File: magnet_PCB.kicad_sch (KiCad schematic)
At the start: 0 parts

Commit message: Add LED strip subsheet and place all components
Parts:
- added BT1: Battery_Cell, symbol Device:Battery_Cell
- added LS1: Speaker, symbol Device:Speaker
- added M5: Motor_DC_ALT, symbol Motor:Motor_DC_ALT
- added RV2: R_Potentiometer_Trim, symbol Device:R_Potentiometer_Trim
- added U1: DRV8833PW, Package_SO:TSSOP-16_4.4x5mm_P0.65mm, symbol Driver_Motor:DRV8833PW
- added U2: MAX98306xDT, Package_DFN_QFN:TDFN-14-1EP_3x3mm_P0.4mm_EP1.78x2.35mm, symbol Amplifier_Audio:MAX98306xDT
- added U3: ESP32-S3, Package_DFN_QFN:QFN-56-1EP_7x7mm_P0.4mm_EP4x4mm, symbol MCU_Espressif:ESP32-S3
- added U4: HC-SR04, Sensor-Ultrasonic:XCVR_HC-SR04, symbol HC-SR04:HC-SR04
- added U5: LT1085-3.3, Package_TO_SOT_SMD:TO-263-2, symbol Regulator_Linear:LT1085-3.3
- added U6: LM2596S-5, Package_TO_SOT_SMD:TO-263-5_TabPin3, symbol Regulator_Switching:LM2596S-5
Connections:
- new net: U2.1 (PGND), U2.15 (PGND), U2.8 (PGND)
- new net: U2.11 (PVDD), U2.12 (PVDD)
- new net: U3.2 (VDD3P3), U3.3 (VDD3P3)
- new net: U3.55 (VDDA), U3.56 (VDDA)
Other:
- added sheet LED_Strip_8 (LED_Strip_8.kicad_sch)

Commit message: Wired LED strip
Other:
- moved on the sheet: BT1
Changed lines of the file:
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@@
 	(symbol
 		(lib_id "Device:Battery_Cell")
-		(at 81.28 161.29 0)
+		(at 57.15 146.05 0)
 		(unit 1)
 		(exclude_from_sim no)
@@
 		(fields_autoplaced yes)
 		(property "Reference" "BT1"
-			(at 85.09 158.1784 0)
+			(at 60.96 142.9384 0)
 			(effects
 				(font
@@
 		)
 		(property "Value" "Battery_Cell"
-			(at 85.09 160.7184 0)
+			(at 60.96 145.4784 0)
 			(effects
 				(font
@@
 		)
 		(property "Footprint" ""
-			(at 81.28 159.766 90)
+			(at 57.15 144.526 90)
 			(effects
 				(font
@@
 		)
 		(property "Datasheet" "~"
-			(at 81.28 159.766 90)
+			(at 57.15 144.526 90)
 			(effects
 				(font
@@
 		)
 		(property "Description" "Single-cell battery"
-			(at 81.28 161.29 0)
+			(at 57.15 146.05 0)
 			(effects
 				(font

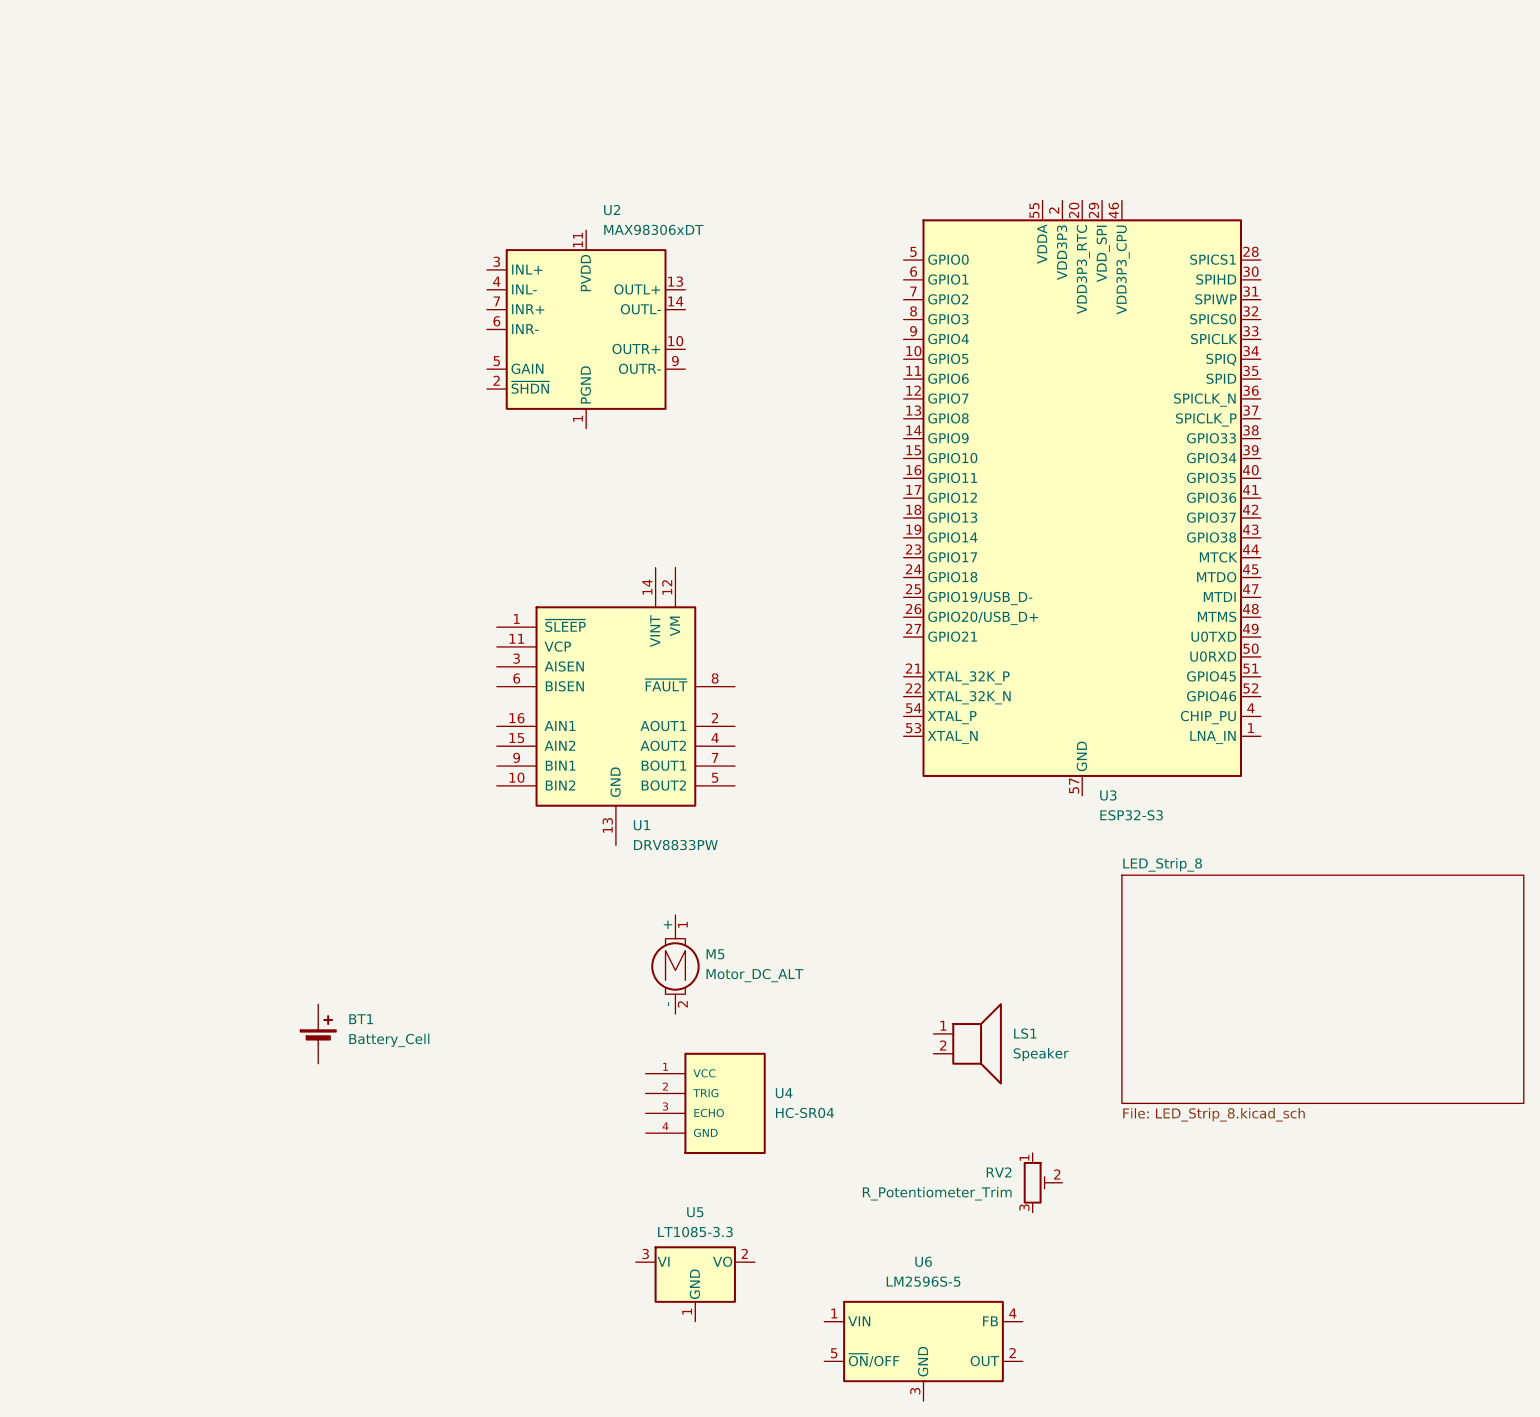
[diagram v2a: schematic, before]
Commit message: Added regulators
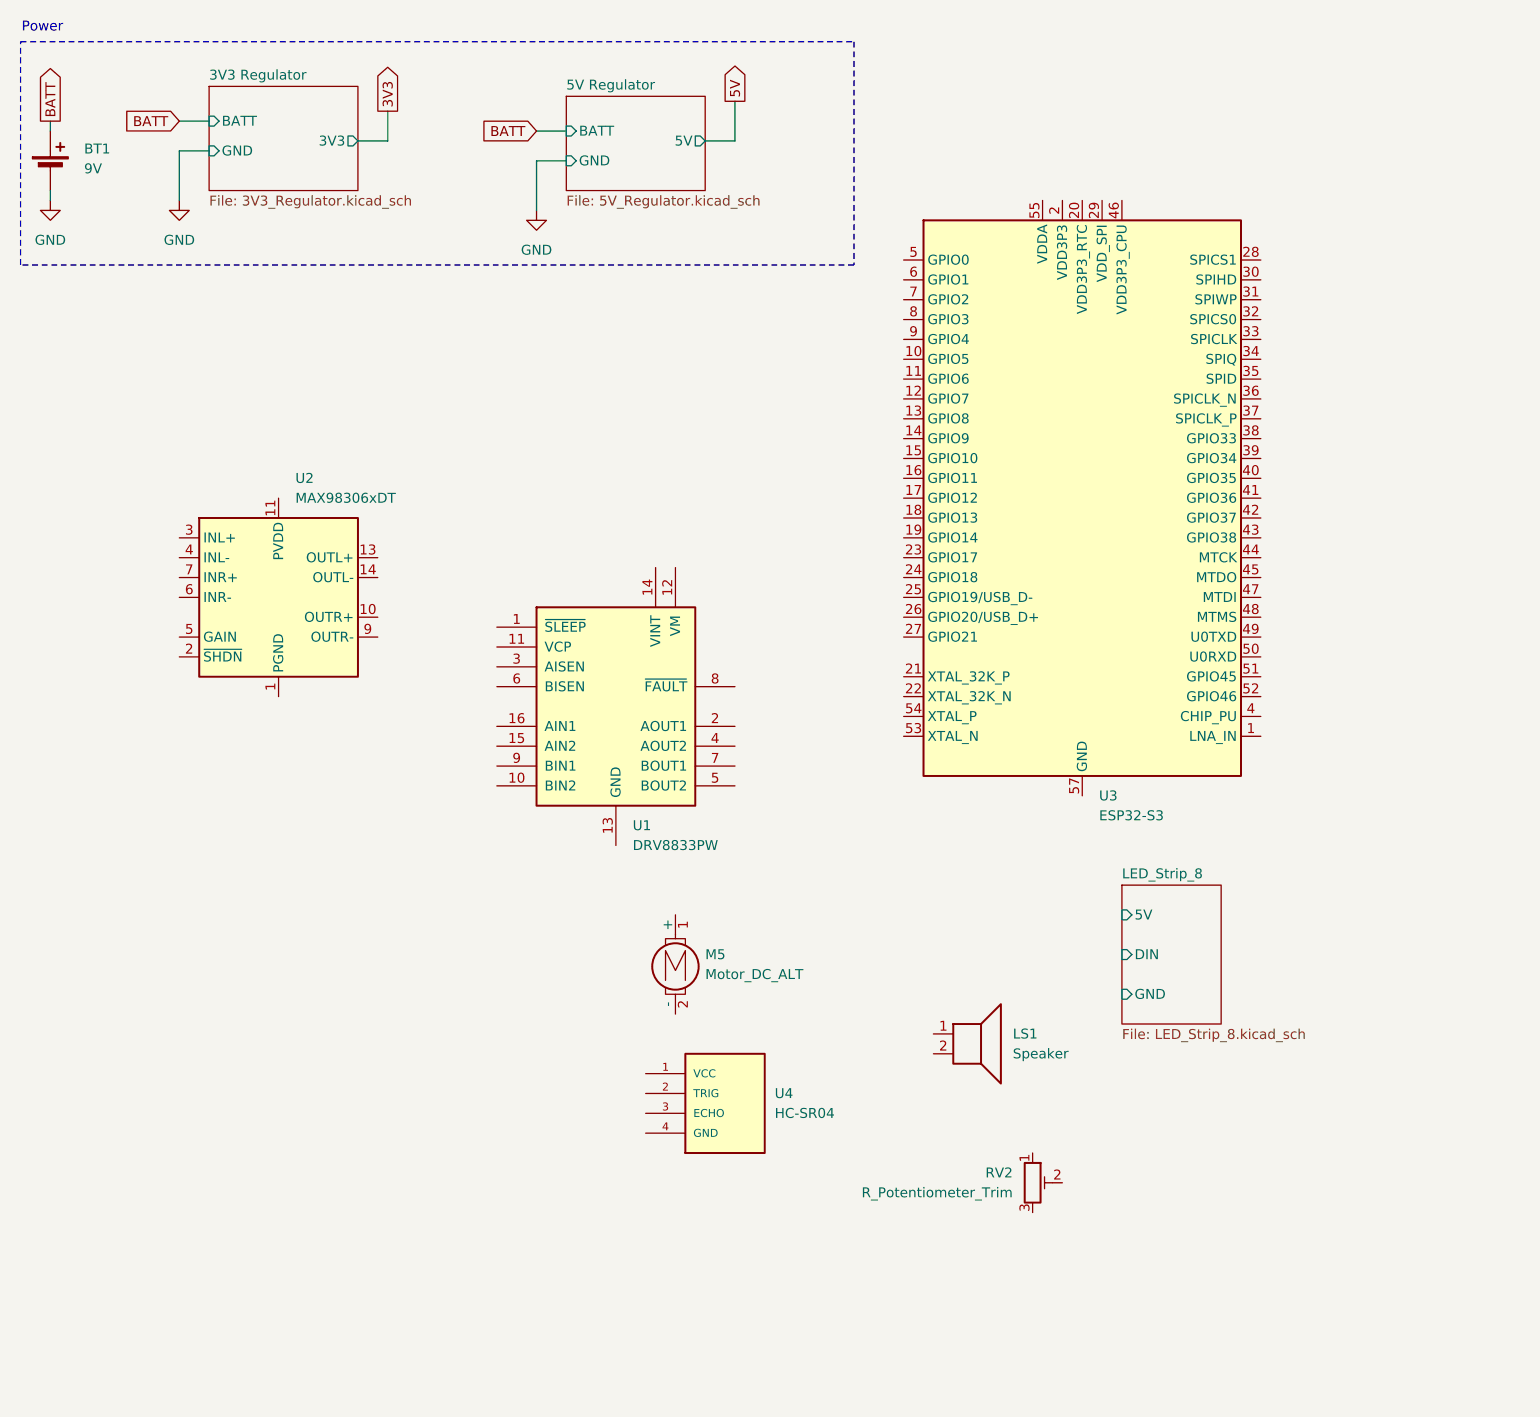
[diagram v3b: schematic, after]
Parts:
- removed U5: LT1085-3.3, Package_TO_SOT_SMD:TO-263-2, symbol Regulator_Linear:LT1085-3.3
- removed U6: LM2596S-5, Package_TO_SOT_SMD:TO-263-5_TabPin3, symbol Regulator_Switching:LM2596S-5
- BT1: value Battery_Cell -> 9V
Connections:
- net BATT: now reaches BT1.1 (+)
- net GND: now reaches BT1.2 (-)
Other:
- added sheet 3V3 Regulator (3V3_Regulator.kicad_sch)
- added sheet 5V Regulator (5V_Regulator.kicad_sch)
- sheet LED_Strip_8 ports: added 5V, DIN, GND; removed none
- note added: "Power"
- moved on the sheet: BT1, U2
